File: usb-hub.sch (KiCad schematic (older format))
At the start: 48 parts, among them J1 USB_C_Receptacle_16pin, J2 USB_C_Receptacle_16pin, J3 USB_C_Receptacle_16pin, P1 CONN_02X03, Q1 Q_PMOS_GSD 2A, Q2 Q_NMOS_GSD 1Amp, Q3 Q_NMOS_GSD 1Amp, Q4 Q_NMOS_GSD 1Amp, Q5 Q_PMOS_GSD 2A, Q6 Q_NMOS_GSD 1Amp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

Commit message: wip neuron layout
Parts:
- removed L3: 470R at 100M, 1A, raise_fp:R_0603, symbol Ferrite_Bead
- removed Q5: Q_PMOS_GSD 2A, raise_fp:SOT-23, symbol Q_PMOS_GSD
- removed Q6: Q_NMOS_GSD 1Amp, raise_fp:SOT-323_SC-70, symbol Q_NMOS_GSD
- removed R7: 10k, 125mW, 5%, raise_fp:R_0603, symbol R
- removed TP1: TEST, raise_fp:testpoint, symbol TEST
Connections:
- net labels added: side-power, side-switch
- net labels removed: left-switch, pwm2_b, pwm2_g, pwm2_r, pwm3_b, pwm3_g, pwm3_r, right-switch, samd-usb_N, samd-usb_P
- wire segments 66 -> 59
- no-connect marks 21 -> 28
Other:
- moved on the sheet: C1, C2, C3, J2, J3, L1, P1, Q1, Q2, R1, TP10, TP11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

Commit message: routed
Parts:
- removed Q3, Q4: Q_NMOS_GSD 1Amp, raise_fp:SOT-323_SC-70, symbol Q_NMOS_GSD
- removed R5: 4.7k, 125mW, 5%, raise_fp:R_0603, symbol R
- removed TP12, TP9: TEST, raise_fp:testpoint, symbol TEST
- removed U2: LY2508, raise_fp:SOT-23, symbol LD1117S12TR_SOT223
- added R11, R12: 1M, 125mW, 5%, raise_fp:R_0603, symbol R
- added R7: 10k, 125mW, 5%, raise_fp:R_0603, symbol R
- added SW1: SW_Push, raise_fp:reset-button, symbol SW_Push
- added TP1, TP6, TP7: TEST, raise_fp:testpoint, symbol TEST
- added U2: LY2508, raise_fp:SOT-23, symbol regulator
- R3: farnell # 1469807 -> 2447230
- R4: value 10k, 125mW, 5% -> 4.7k, 125mW, 5%; MOQ (none) -> Value; leadtime (none) -> Value; supplier PN (none) -> Value
- U1: MOQ (none) -> Value; leadtime (none) -> Value; supplier (none) -> STMicroElectronics; supplier PN (none) -> USBLC6-4SC6
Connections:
- net labels removed: scl5, sda5
- wire segments 59 -> 53
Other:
- note added: "6 pin SWD ARM pinout"
- note added: "\nsamd21 with 1 RGBs: 5mA"
- note removed: "https://www.nxp.com/docs/en/application-note/AN10441.pdf"
- note removed: "level translate\n"
- note removed: "usb hub: 65mA\nsamd21 with 3 RGBs: 10mA"
- moved on the sheet: P1, R10, R8, R9, U1, U4

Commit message: added holes
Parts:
- added J4, J5, J6, J7: Conn_01x01_Female, raise_fp:Fiducial_0.5mm_Dia_1mm_Outer, symbol Conn_01x01_Female
- added R13, R5: 36k, 125mW, 5%, raise_fp:R_0603, symbol R
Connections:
- net +3V3: now also R13.1, R5.1
- net dfp-l-cc: now also R13.2
- net dfp-r-cc: now also R5.2
- no-connect marks 28 -> 32
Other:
- note added: "dfp pull up/down"
- note added: "fiducials"
- moved on the sheet: R11, R12
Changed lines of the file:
@@
 L R R11
 U 1 1 5B164F68
-P 750 3550
-F 0 "R11" V 830 3550 50  0000 C CNN
-F 1 "1M, 125mW, 5%" V 900 3600 50  0000 C CNN
-F 2 "raise_fp:R_0603" V 680 3550 30  0001 C CNN
-F 3 "" H 750 3550 30  0000 C CNN
-F 4 "2073351" H 750 3550 60  0001 C CNN "farnell #"
-F 5 "any/open" H -3750 50  60  0001 C CNN "supplier"
-F 6 "Value" H 750 3550 60  0001 C CNN "supplier PN"
-F 7 "Value" H 750 3550 60  0001 C CNN "MOQ"
-F 8 "Value" H 750 3550 60  0001 C CNN "leadtime"
-	1    750  3550
+P 8200 4400
+F 0 "R11" V 8280 4400 50  0000 C CNN
+F 1 "1M, 125mW, 5%" V 8350 4450 50  0000 C CNN
+F 2 "raise_fp:R_0603" V 8130 4400 30  0001 C CNN
+F 3 "" H 8200 4400 30  0000 C CNN
+F 4 "2073351" H 8200 4400 60  0001 C CNN "farnell #"
+F 5 "any/open" H 3700 900 60  0001 C CNN "supplier"
+F 6 "Value" H 8200 4400 60  0001 C CNN "supplier PN"
+F 7 "Value" H 8200 4400 60  0001 C CNN "MOQ"
+F 8 "Value" H 8200 4400 60  0001 C CNN "leadtime"
+	1    8200 4400
 	1    0    0    -1
 $EndComp
@@
 L Earth #PWR049
 U 1 1 5B1650D8
-P 750 3700
-F 0 "#PWR049" H 750 3450 50  0001 C CNN
-F 1 "Earth" H 750 3550 50  0001 C CNN
-F 2 "" H 750 3700 60  0000 C CNN
-F 3 "" H 750 3700 60  0000 C CNN
-	1    750  3700
+P 8200 4550
+F 0 "#PWR049" H 8200 4300 50  0001 C CNN
+F 1 "Earth" H 8200 4400 50  0001 C CNN
+F 2 "" H 8200 4550 60  0000 C CNN
+F 3 "" H 8200 4550 60  0000 C CNN
+	1    8200 4550
 	1    0    0    -1
 $EndComp
@@
 L Earth #PWR052
 U 1 1 5B165141
-P 950 3700
-F 0 "#PWR052" H 950 3450 50  0001 C CNN
-F 1 "Earth" H 950 3550 50  0001 C CNN
-F 2 "" H 950 3700 60  0000 C CNN
-F 3 "" H 950 3700 60  0000 C CNN
-	1    950  3700
+P 8750 4550
+F 0 "#PWR052" H 8750 4300 50  0001 C CNN
+F 1 "Earth" H 8750 4400 50  0001 C CNN
+F 2 "" H 8750 4550 60  0000 C CNN
+F 3 "" H 8750 4550 60  0000 C CNN
+	1    8750 4550
 	1    0    0    -1
 $EndComp
@@
 L R R12
 U 1 1 5B165592
-P 950 3550
-F 0 "R12" V 1030 3550 50  0000 C CNN
-F 1 "1M, 125mW, 5%" V 1100 3600 50  0000 C CNN
-F 2 "raise_fp:R_0603" V 880 3550 30  0001 C CNN
-F 3 "" H 950 3550 30  0000 C CNN
-F 4 "2073351" H 950 3550 60  0001 C CNN "farnell #"
-F 5 "any/open" H -3550 50  60  0001 C CNN "supplier"
-F 6 "Value" H 950 3550 60  0001 C CNN "supplier PN"
-F 7 "Value" H 950 3550 60  0001 C CNN "MOQ"
-F 8 "Value" H 950 3550 60  0001 C CNN "leadtime"
-	1    950  3550
-	1    0    0    -1
-$EndComp
-Text Label 750  3400 1    60   ~ 0
+P 8750 4400
+F 0 "R12" V 8830 4400 50  0000 C CNN
+F 1 "1M, 125mW, 5%" V 8900 4450 50  0000 C CNN
+F 2 "raise_fp:R_0603" V 8680 4400 30  0001 C CNN
+F 3 "" H 8750 4400 30  0000 C CNN
+F 4 "2073351" H 8750 4400 60  0001 C CNN "farnell #"
+F 5 "any/open" H 4250 900 60  0001 C CNN "supplier"
+F 6 "Value" H 8750 4400 60  0001 C CNN "supplier PN"
+F 7 "Value" H 8750 4400 60  0001 C CNN "MOQ"
+F 8 "Value" H 8750 4400 60  0001 C CNN "leadtime"
+	1    8750 4400
+	1    0    0    -1
+$EndComp
+Text Label 8200 4250 2    60   ~ 0
 dfp-r-cc
-Text Label 950  3400 1    60   ~ 0
+Text Label 8750 4250 2    60   ~ 0
 dfp-l-cc
 Text Notes 4950 3250 0    60   ~ 0
@@
 Text Label 7200 4350 3    60   ~ 0
 scl
+$Comp
+L R R5
+U 1 1 5B30E926
+P 8200 4100
+F 0 "R5" V 8280 4100 50  0000 C CNN
+F 1 "36k, 125mW, 5%" V 8350 4150 50  0000 C CNN
+F 2 "raise_fp:R_0603" V 8130 4100 30  0001 C CNN
+F 3 "" H 8200 4100 30  0000 C CNN
+F 4 "2447349" H 8200 4100 60  0001 C CNN "farnell #"
+F 5 "any/open" H 3700 600 60  0001 C CNN "supplier"
+F 6 "Value" H 8200 4100 60  0001 C CNN "supplier PN"
+F 7 "Value" H 8200 4100 60  0001 C CNN "MOQ"
+F 8 "Value" H 8200 4100 60  0001 C CNN "leadtime"
+	1    8200 4100
+	1    0    0    -1
+$EndComp
+$Comp
+L R R13
+U 1 1 5B30E9DE
+P 8750 4100
+F 0 "R13" V 8830 4100 50  0000 C CNN
+F 1 "36k, 125mW, 5%" V 8900 4150 50  0000 C CNN
+F 2 "raise_fp:R_0603" V 8680 4100 30  0001 C CNN
+F 3 "" H 8750 4100 30  0000 C CNN
+F 4 "2447349" H 8750 4100 60  0001 C CNN "farnell #"
+F 5 "any/open" H 4250 600 60  0001 C CNN "supplier"
+F 6 "Value" H 8750 4100 60  0001 C CNN "supplier PN"
+F 7 "Value" H 8750 4100 60  0001 C CNN "MOQ"
+F 8 "Value" H 8750 4100 60  0001 C CNN "leadtime"
+	1    8750 4100
+	1    0    0    -1
+$EndComp
+$Comp
+L +3.3V #PWR026
+U 1 1 5B30ED4A
+P 8750 3950
+F 0 "#PWR026" H 8750 3800 50  0001 C CNN
+F 1 "+3.3V" V 8765 4078 50  0000 L CNN
+F 2 "" H 8750 3950 50  0001 C CNN
+F 3 "" H 8750 3950 50  0001 C CNN
+	1    8750 3950
+	1    0    0    -1
+$EndComp
+$Comp
+L +3.3V #PWR027
+U 1 1 5B30EDE2
+P 8200 3950
+F 0 "#PWR027" H 8200 3800 50  0001 C CNN
+F 1 "+3.3V" V 8215 4078 50  0000 L CNN
+F 2 "" H 8200 3950 50  0001 C CNN
+F 3 "" H 8200 3950 50  0001 C CNN
+	1    8200 3950
+	1    0    0    -1
+$EndComp
+Text Notes 8100 3500 0    60   ~ 0
+dfp pull up/down
+$Comp
+L Conn_01x01_Female J5
+U 1 1 5B310461
+P 8850 2150
+F 0 "J5" H 8877 2176 50  0000 L CNN
+F 1 "Conn_01x01_Female" H 8877 2085 50  0000 L CNN
+F 2 "raise_fp:Fiducial_0.5mm_Dia_1mm_Outer" H 8850 2150 50  0001 C CNN
+F 3 "~" H 8850 2150 50  0001 C CNN
+	1    8850 2150
+	1    0    0    -1
+$EndComp
+NoConn ~ 8650 2150
+$Comp
+L Conn_01x01_Female J4
+U 1 1 5B310711
+P 8850 2050
+F 0 "J4" H 8877 2076 50  0000 L CNN
+F 1 "Conn_01x01_Female" H 8877 1985 50  0000 L CNN
+F 2 "raise_fp:Fiducial_0.5mm_Dia_1mm_Outer" H 8850 2050 50  0001 C CNN
+F 3 "~" H 8850 2050 50  0001 C CNN
+	1    8850 2050
+	1    0    0    -1
+$EndComp
+NoConn ~ 8650 2050
+$Comp
+L Conn_01x01_Female J7
+U 1 1 5B3107E3
+P 8850 2350
+F 0 "J7" H 8877 2376 50  0000 L CNN
+F 1 "Conn_01x01_Female" H 8877 2285 50  0000 L CNN
+F 2 "raise_fp:Fiducial_0.5mm_Dia_1mm_Outer" H 8850 2350 50  0001 C CNN
+F 3 "~" H 8850 2350 50  0001 C CNN
+	1    8850 2350
+	1    0    0    -1
+$EndComp
+NoConn ~ 8650 2350
+$Comp
+L Conn_01x01_Female J6
+U 1 1 5B3107EA
+P 8850 2250
+F 0 "J6" H 8877 2276 50  0000 L CNN
+F 1 "Conn_01x01_Female" H 8877 2185 50  0000 L CNN
+F 2 "raise_fp:Fiducial_0.5mm_Dia_1mm_Outer" H 8850 2250 50  0001 C CNN
+F 3 "~" H 8850 2250 50  0001 C CNN
+	1    8850 2250
+	1    0    0    -1
+$EndComp
+NoConn ~ 8650 2250
+Text Notes 8600 1850 0    60   ~ 0
+fiducials
 $EndSCHEMATC

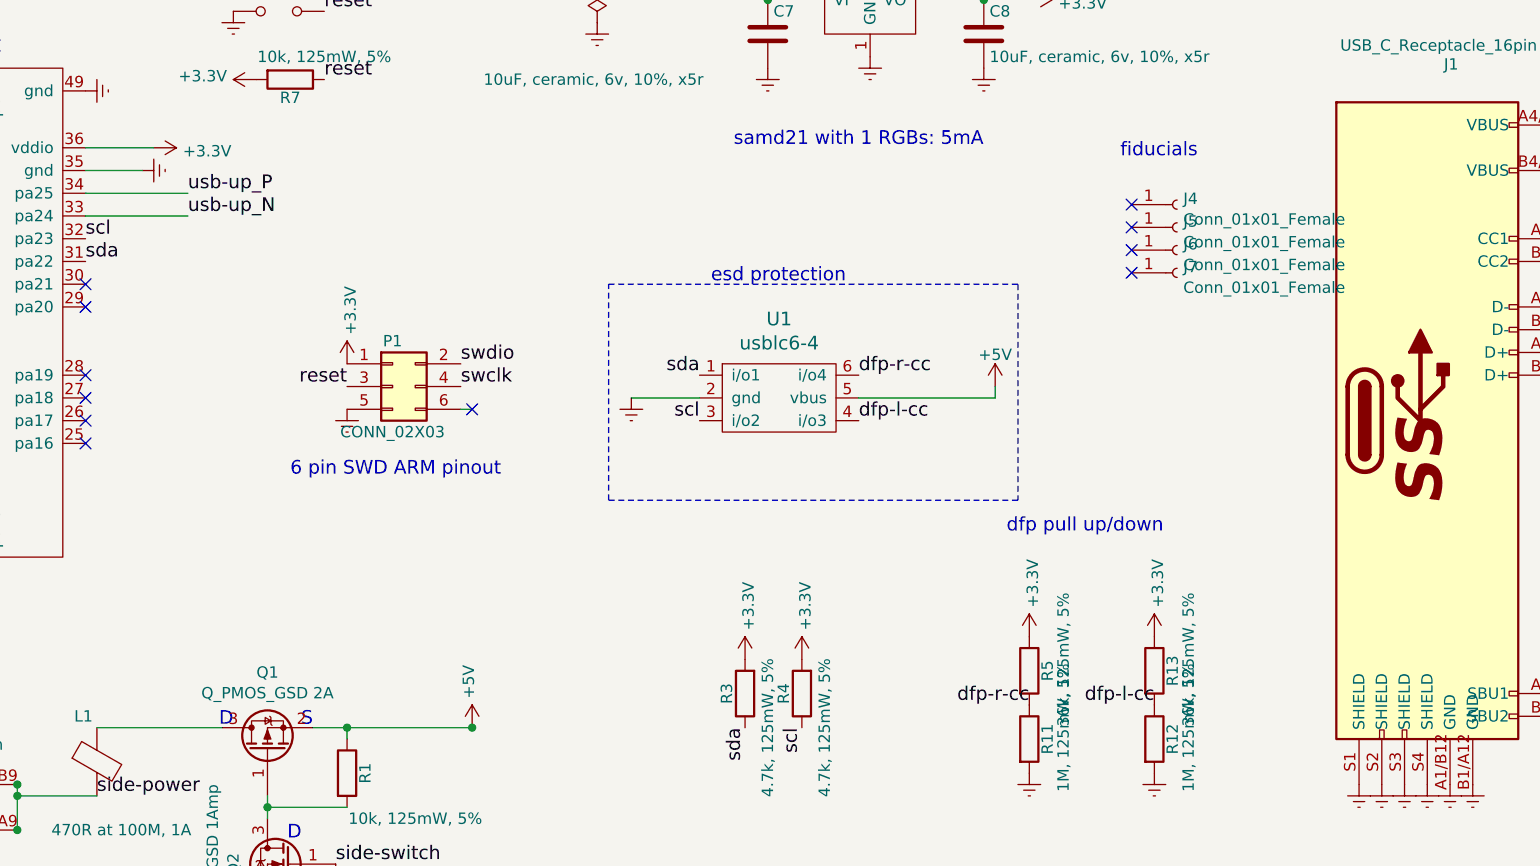
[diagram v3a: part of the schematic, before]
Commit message: ansi/iso bom
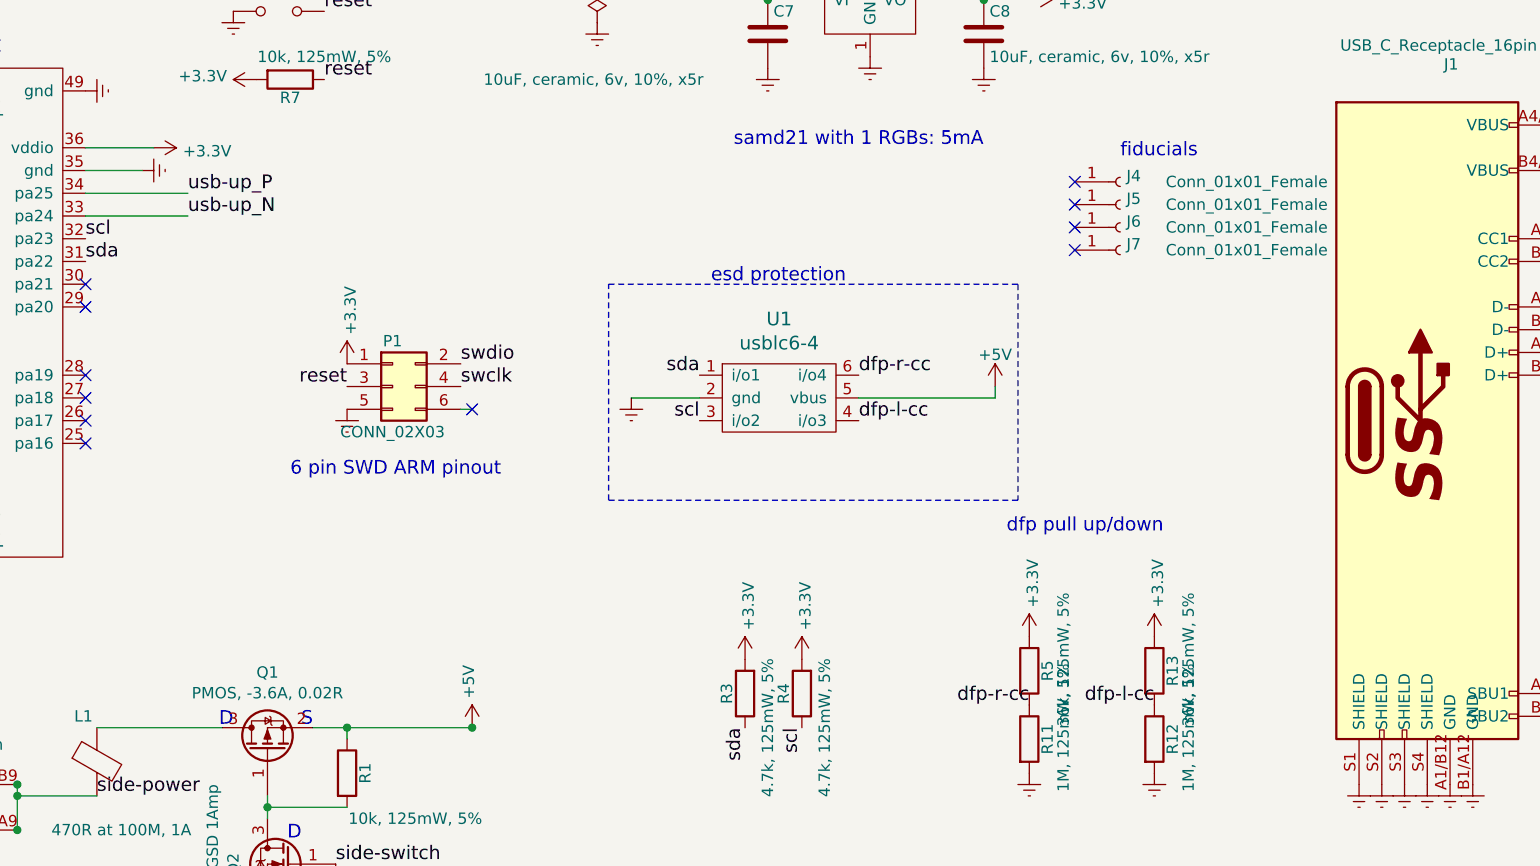
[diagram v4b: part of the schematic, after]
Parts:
- J4: MOQ (none) -> Value; dnp (none) -> dnp; leadtime (none) -> Value; supplier (none) -> dnp; supplier PN (none) -> Value
- J5, J6, J7: MOQ (none) -> Value; leadtime (none) -> Value; supplier (none) -> dnp; supplier PN (none) -> dnp
- L1, L2: supplier any/open -> Murata; supplier PN Value -> BLM18PG471SN1D
- Q1: value Q_PMOS_GSD 2A -> PMOS, -3.6A, 0.02R
- Q2: supplier any/open -> Diodes Inc.; supplier PN Value -> DMG1012UW
- SW1: MOQ (none) -> Value; leadtime (none) -> Value; supplier (none) -> DONGGUAN WEIKAI ELECTRONIC CO.,LTD; supplier PN (none) -> TS20AB65A20B011
- U4: value 4 pin RGB led, com anode, red: 500mcd 620nm. Green: 1000mcd 520nm. Blue: 500mcd 460nm. -> 4 pin RGB led, com anode
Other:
- moved on the sheet: J4, J5, J6, J7

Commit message: fixes for gp
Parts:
- removed R13, R5: 36k, 125mW, 5%, raise_fp:R_0603, symbol R
- added TP12, TP9: TEST, raise_fp:testpoint, symbol TEST
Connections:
- net scl: now also TP12.1
- net sda: now also TP9.1
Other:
- note added: "dfp pull down"
- note added: "i2c pullups"
- note removed: "dfp pull up/down"
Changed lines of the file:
@@
 encoding utf-8
 Sheet 1 1
-Title ""
-Date ""
-Rev ""
-Comp ""
+Title "Huble"
+Date "2018-07-25"
+Rev "v3.1"
+Comp "Dygma"
 Comment1 ""
 Comment2 ""
@@
 Text Label 7200 4350 3    60   ~ 0
 scl
-$Comp
-L R R5
-U 1 1 5B30E926
-P 8200 4100
-F 0 "R5" V 8280 4100 50  0000 C CNN
-F 1 "36k, 125mW, 5%" V 8350 4150 50  0000 C CNN
-F 2 "raise_fp:R_0603" V 8130 4100 30  0001 C CNN
-F 3 "" H 8200 4100 30  0000 C CNN
-F 4 "2447349" H 8200 4100 60  0001 C CNN "farnell #"
-F 5 "any/open" H 3700 600 60  0001 C CNN "supplier"
-F 6 "Value" H 8200 4100 60  0001 C CNN "supplier PN"
-F 7 "Value" H 8200 4100 60  0001 C CNN "MOQ"
-F 8 "Value" H 8200 4100 60  0001 C CNN "leadtime"
-	1    8200 4100
-	1    0    0    -1
-$EndComp
-$Comp
-L R R13
-U 1 1 5B30E9DE
-P 8750 4100
-F 0 "R13" V 8830 4100 50  0000 C CNN
-F 1 "36k, 125mW, 5%" V 8900 4150 50  0000 C CNN
-F 2 "raise_fp:R_0603" V 8680 4100 30  0001 C CNN
-F 3 "" H 8750 4100 30  0000 C CNN
-F 4 "2447349" H 8750 4100 60  0001 C CNN "farnell #"
-F 5 "any/open" H 4250 600 60  0001 C CNN "supplier"
-F 6 "Value" H 8750 4100 60  0001 C CNN "supplier PN"
-F 7 "Value" H 8750 4100 60  0001 C CNN "MOQ"
-F 8 "Value" H 8750 4100 60  0001 C CNN "leadtime"
-	1    8750 4100
-	1    0    0    -1
-$EndComp
-$Comp
-L +3.3V #PWR026
-U 1 1 5B30ED4A
-P 8750 3950
-F 0 "#PWR026" H 8750 3800 50  0001 C CNN
-F 1 "+3.3V" V 8765 4078 50  0000 L CNN
-F 2 "" H 8750 3950 50  0001 C CNN
-F 3 "" H 8750 3950 50  0001 C CNN
-	1    8750 3950
-	1    0    0    -1
-$EndComp
-$Comp
-L +3.3V #PWR027
-U 1 1 5B30EDE2
-P 8200 3950
-F 0 "#PWR027" H 8200 3800 50  0001 C CNN
-F 1 "+3.3V" V 8215 4078 50  0000 L CNN
-F 2 "" H 8200 3950 50  0001 C CNN
-F 3 "" H 8200 3950 50  0001 C CNN
-	1    8200 3950
-	1    0    0    -1
-$EndComp
-Text Notes 8100 3500 0    60   ~ 0
-dfp pull up/down
+Text Notes 8200 3900 0    60   ~ 0
+dfp pull down
 $Comp
 L Conn_01x01_Female J5
@@
 Text Notes 8600 1850 0    60   ~ 0
 fiducials
+Text Label 9650 6150 0    60   ~ 0
+sda
+Text Label 9650 6250 0    60   ~ 0
+scl
+$Comp
+L TEST TP12
+U 1 1 5B585703
+P 9650 6250
+F 0 "TP12" H 9728 6390 50  0000 L CNN
+F 1 "TEST" H 9750 6250 50  0000 L CNN
+F 2 "raise_fp:testpoint" H 9650 6250 50  0001 C CNN
+F 3 "" H 9650 6250 50  0001 C CNN
+F 4 "dnp" H 3350 1750 60  0001 C CNN "farnell #"
+F 5 "dnp" H 3350 1750 60  0001 C CNN "supplier"
+	1    9650 6250
+	0    -1   -1   0
+$EndComp
+$Comp
+L TEST TP9
+U 1 1 5B58578D
+P 9650 6150
+F 0 "TP9" H 9728 6290 50  0000 L CNN
+F 1 "TEST" H 9750 6150 50  0000 L CNN
+F 2 "raise_fp:testpoint" H 9650 6150 50  0001 C CNN
+F 3 "" H 9650 6150 50  0001 C CNN
+F 4 "dnp" H 3350 1650 60  0001 C CNN "farnell #"
+F 5 "dnp" H 3350 1650 60  0001 C CNN "supplier"
+	1    9650 6150
+	0    -1   -1   0
+$EndComp
+Text Notes 6850 3650 0    60   ~ 0
+i2c pullups
+Wire Notes Line
+	6650 3450 7550 3450
+Wire Notes Line
+	7550 3450 7550 4850
+Wire Notes Line
+	7550 4850 6600 4850
+Wire Notes Line
+	6600 4850 6600 3450
+Wire Notes Line
+	6600 3450 6700 3450
+Wire Notes Line
+	7700 3450 9100 3450
+Wire Notes Line
+	9100 3450 9100 4850
+Wire Notes Line
+	9100 4850 7700 4850
+Wire Notes Line
+	7700 4850 7700 3450
+Wire Notes Line
+	5000 2250 6200 2250
+Wire Notes Line
+	6200 2250 6200 3350
+Wire Notes Line
+	6200 3350 4850 3350
+Wire Notes Line
+	4850 3350 4850 2250
+Wire Notes Line
+	4850 2250 5050 2250
 $EndSCHEMATC
